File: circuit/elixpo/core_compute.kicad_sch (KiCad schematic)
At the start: 19 parts, among them SW1 RESET, SW2 BOOT, U1 ESP32-S3R8, U2 W25Q128JVSIQ 16MB, Y1 40MHz 10pF

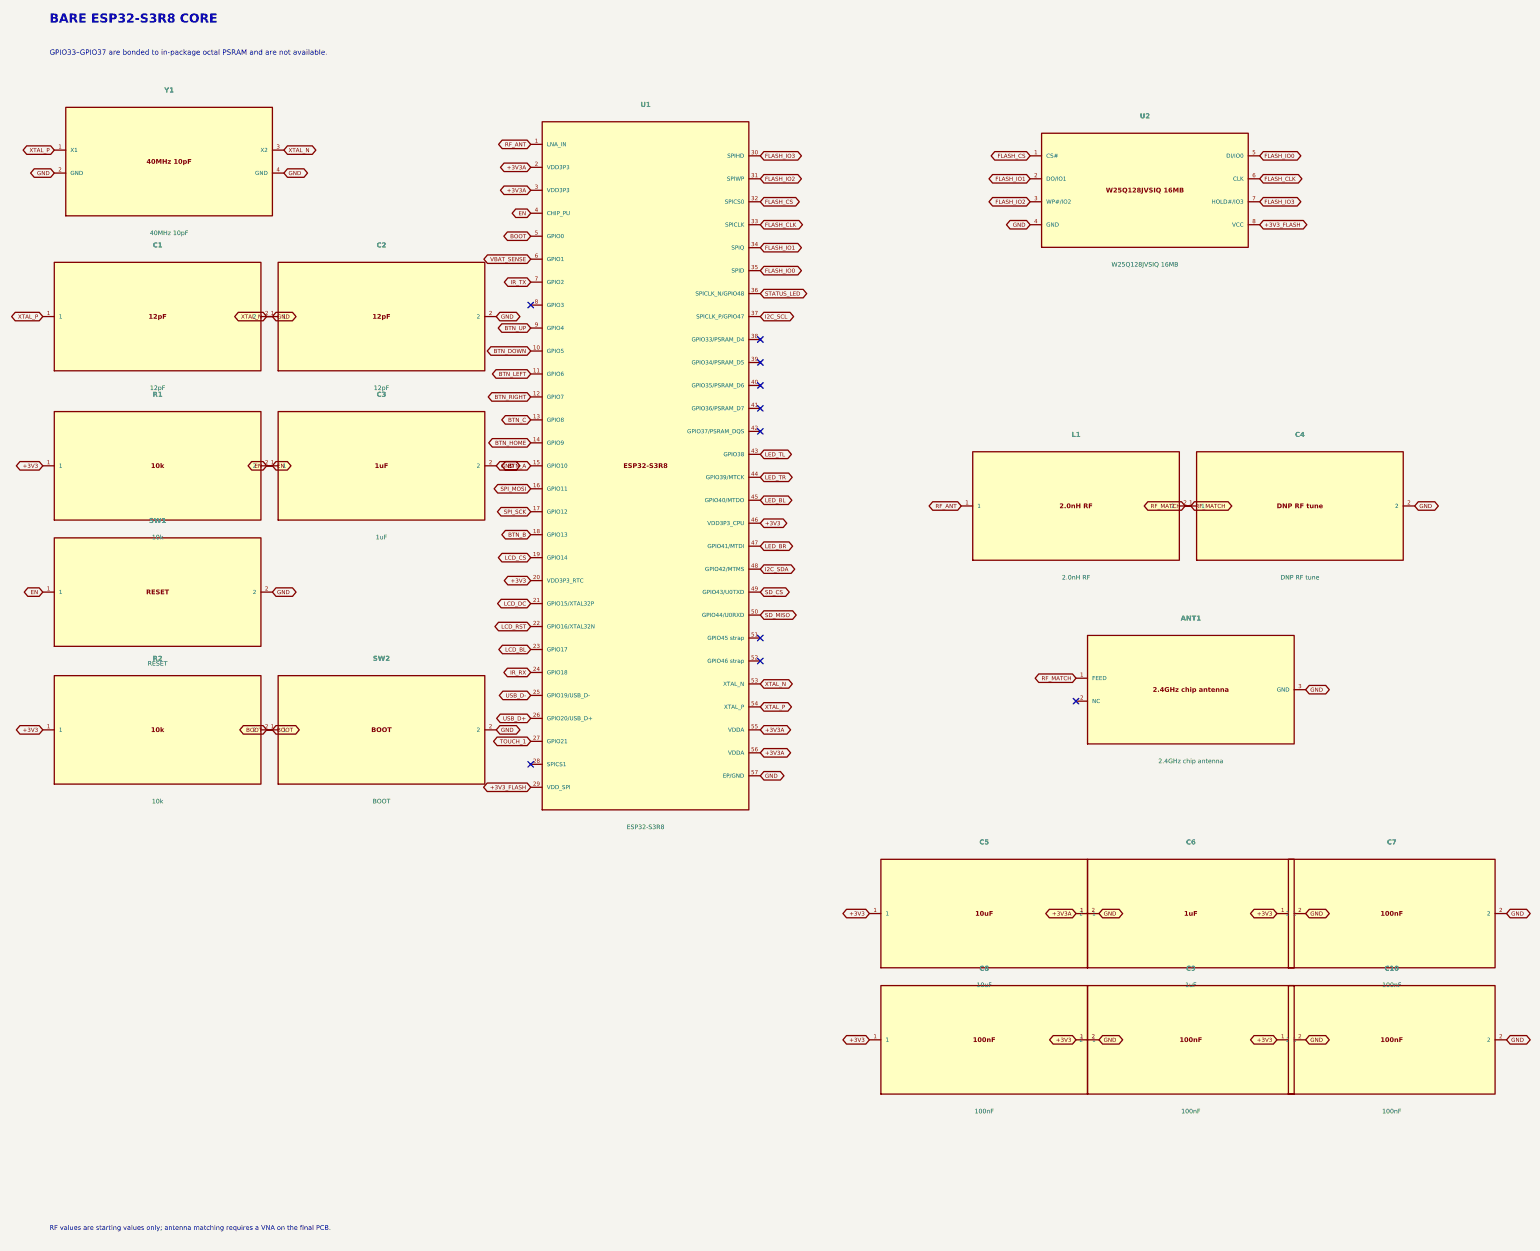
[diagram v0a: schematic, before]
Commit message: feat(hardware): complete badge schematic and procurement BOM
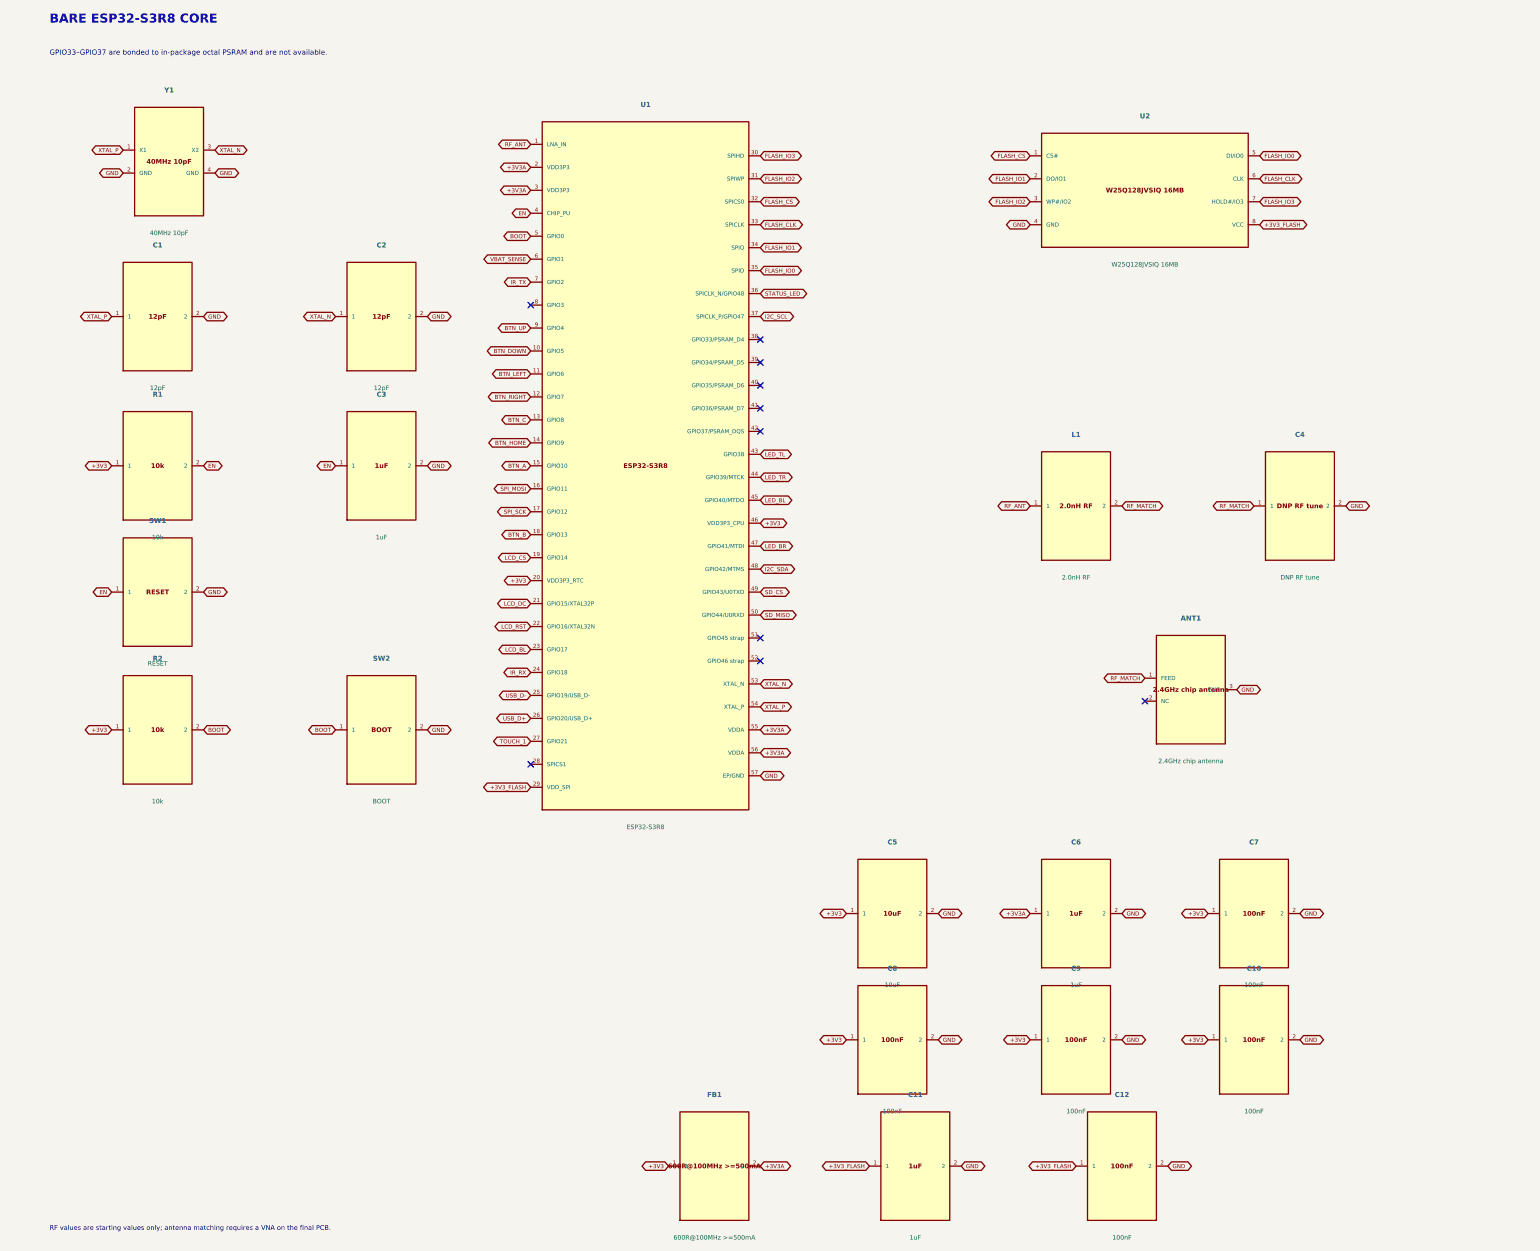
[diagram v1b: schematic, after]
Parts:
- added C11: 1uF, Capacitor_SMD:C_0603_1608Metric, symbol oreo_badge:C11
- added C12: 100nF, Capacitor_SMD:C_0402_1005Metric, symbol oreo_badge:C12
- added FB1: 600R@100MHz >=500mA, Inductor_SMD:L_0603_1608Metric, symbol oreo_badge:FB1
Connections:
- net +3V3: now also FB1.1
- net +3V3A: now also FB1.2
- net +3V3_FLASH: now also C11.1, C12.1
- net GND: now also C11.2, C12.2
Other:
- moved on the sheet: C10, C5, C6, C7, C8, C9
